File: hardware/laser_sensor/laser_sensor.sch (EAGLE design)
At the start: 1 part, among them IC1 LM555D

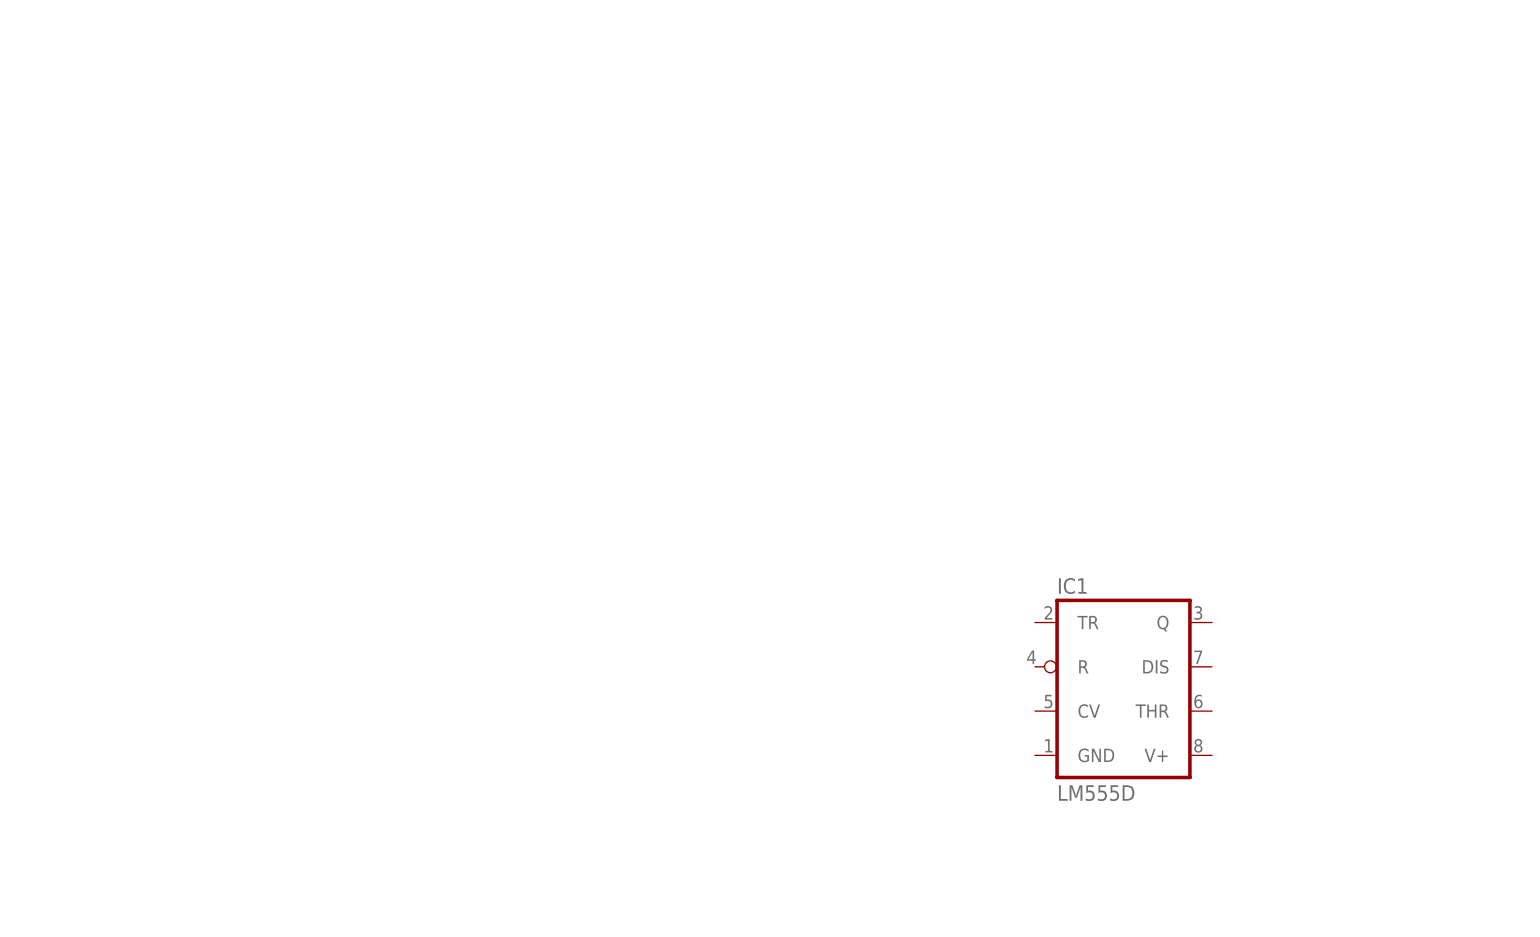
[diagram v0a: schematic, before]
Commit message: First complete route for laser sensor
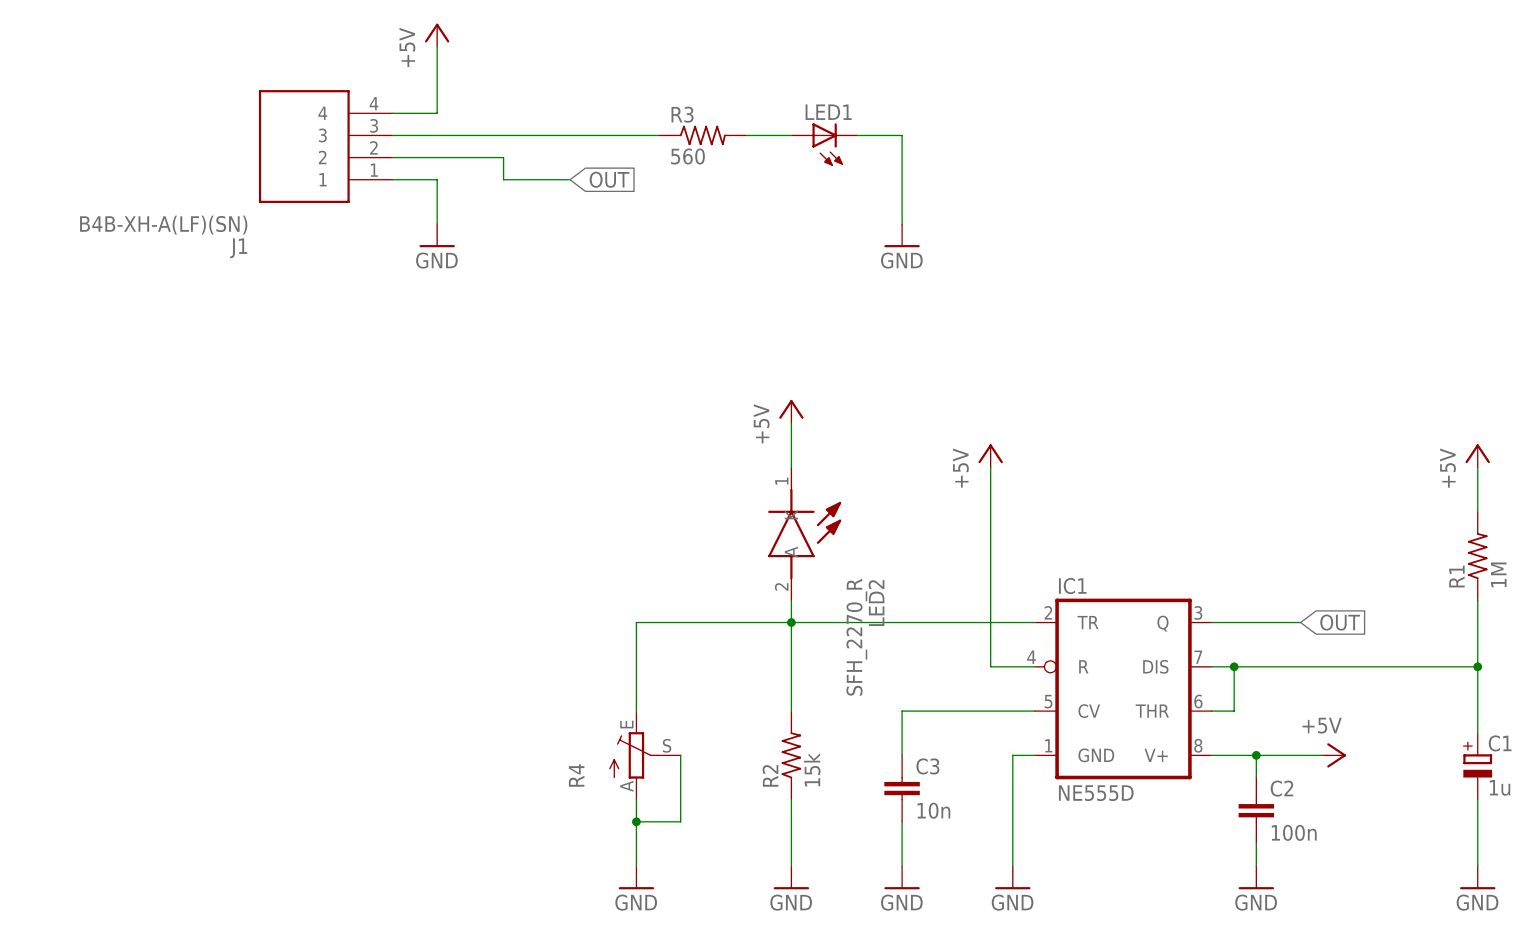
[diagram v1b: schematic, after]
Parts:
- added C1: 1u, rcl:CPOL-EU153CLV-0405
- added C2: 100n, rcl:C-EUC0603K
- added C3: 10n, rcl:C-EUC0805K
- added J1: B4B-XH-A(LF)(SN), B4B-XH-A(LF)(SN):B4B-XH-A(LF)(SN)
- added LED1: (no value), led:LED3MM
- added LED2: SFH_2270_R, SFH_2270_R:SFH_2270_R
- added R1: 1M, resistor:R-US_M0805
- added R2: 15k, resistor:R-US_M0805
- added R3: 560, resistor:R-US_M0805
- added R4: (no value), pot:TRIM_EU-B64Y
- IC1: value LM555D -> NE555D; device linear:LM555D -> linear:NE555D
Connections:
- new net +5V: C2.1, IC1.R, IC1.V+, J1.4, LED2.K, R1.2
- new net GND: C1.-, C2.2, C3.2, IC1.GND, J1.1, LED1.C, R2.1, R4.A, R4.S
- new net N$1: C1.+, IC1.DIS, IC1.THR, R1.1
- new net N$2: J1.3, R3.1
- new net N$3: IC1.TR, LED2.A, R2.2, R4.E
- new net N$4: C3.1, IC1.CV
- new net N$5: LED1.A, R3.2
- new net OUT: IC1.Q, J1.2

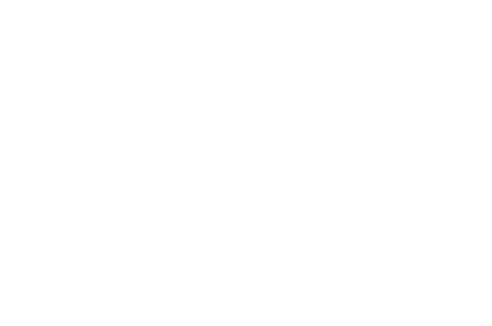
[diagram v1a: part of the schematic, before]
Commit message: Laser sensor gerber updated
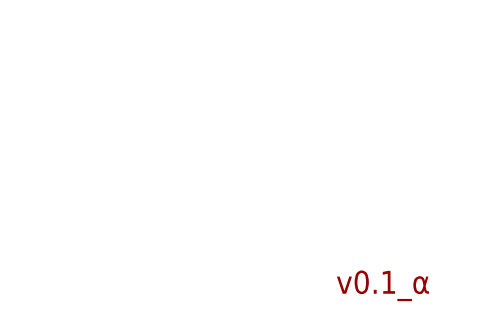
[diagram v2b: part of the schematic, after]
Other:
- note added: "v0.1_α"
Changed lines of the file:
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@@
 <?xml version="1.0" encoding="utf-8"?>
 <!DOCTYPE eagle SYSTEM "eagle.dtd">
-<eagle version="9.1.0">
+<eagle version="9.1.3">
 <drawing>
 <settings>
@@
 <sheet>
 <plain>
+<text x="246.38" y="5.08" size="2.54" layer="94">v0.1_α</text>
 </plain>
 <instances>

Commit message: sensor redesign
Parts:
- removed C1: 1u, rcl:CPOL-EU153CLV-0405
- removed C2: 100n, rcl:C-EUC0603K
- removed C3: 10n, rcl:C-EUC0805K
- removed IC1: NE555D, linear:NE555D
- removed LED2: SFH_2270_R, SFH_2270_R:SFH_2270_R
- added D1: SFH_2440_L, SFH_2440_L:SFH_2440_L
- added Q1: BC817-16LT1SMD, transistor-npn:BC817-16LT1SMD
- R1: value 1M -> 100k; device resistor:R-US_M0805 -> rcl:R-US_R0603
- R2: value 15k -> 100k; device resistor:R-US_M0805 -> rcl:R-US_R0603
- R3: value 560 -> 10k; device resistor:R-US_M0805 -> rcl:R-US_R0603
- R4: value (none) -> 560; device pot:TRIM_EU-B64Y -> rcl:R-US_R0603
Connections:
- net N$2 renamed LED
- removed net N$4: C3.1, IC1.CV
- removed net N$5: LED1.A, R3.2
- new net N$2: LED1.C, Q1.C
- net +5V: now also D1.ANODE, R4.2; no longer C2.1, IC1.R, IC1.V+, LED2.K, R1.2
- net GND: now also Q1.E, R1.2, R2.2; no longer C1.-, C2.2, C3.2, IC1.GND, LED1.C, R2.1, R4.A, R4.S
- net N$1: now also LED1.A, R4.1; no longer C1.+, IC1.DIS, IC1.THR, R1.1
- net N$3: now also Q1.B, R2.1, R3.2; no longer IC1.TR, LED2.A, R2.2, R4.E
- net OUT: now also D1.CATHODE, R1.1; no longer IC1.Q
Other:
- moved on the sheet: LED1, R1, R2, R3
